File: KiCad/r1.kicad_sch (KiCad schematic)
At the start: 73 parts, among them J1 KEYBOARD, J2 VIDEO OUT, J3 ATX-20, J4 DE9_Socket, J5 R1 EXPANSION, Q1 2N4401, SW1 RESET, SW2 CLEAR, U1 6502, U10 74LS245, U11 MAX232, U2 6821, U3 27C64, U4 HM62256BLP, U5 74LS138, U6 74LS00, U7 74LS04, U8 P8X32A-D40, U9 24LC256, X1 1 MHz, X2 5MHz

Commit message: Unzipped and rearranged directories
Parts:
- added C21: 100, Capacitor_THT:CP_Radial_D10.0mm_P5.00mm, symbol Device:C_Polarized
- added C22: 100, Capacitor_THT:CP_Radial_D5.0mm_P2.50mm, symbol Device:C_Polarized
- added S1: ON/OFF, Button_Switch_THT:SW_PUSH_6mm, symbol Switch:SW_DPST
- D1: value LED -> POWER; footprint (none) -> LED_THT:LED_D5.0mm
- JP1, JP2: footprint (none) -> TestPoint:TestPoint_Bridge_Pitch2.54mm_Drill1.0mm
- S3: renamed from SW2; footprint (none) -> Button_Switch_THT:SW_PUSH_6mm
- renumbered SW1 to S2
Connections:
- net -12V: now also J3.12 (-12V), J5.1 (Pin_1), C22.2
- net A0: now also J5.4 (Pin_4), U3.10 (A0), U4.10 (A0)
- net A1: now also J5.24 (Pin_24), U3.9 (A1), U4.9 (A1)
- net A10: now also J5.9 (Pin_9), U3.21 (A10), U4.21 (A10)
- net A11: now also J5.29 (Pin_29), U3.23 (A11), U4.23 (A11)
- net A12: now also J5.10 (Pin_10), U3.2 (A12), U4.2 (A12), U5.1 (A0)
- net A13: now also J5.30 (Pin_30), U4.26 (A13), U5.2 (A1)
- net A14: now also J5.11 (Pin_11), U4.1 (A14), U5.3 (A2)
- net A15: now also J5.31 (Pin_31), U4.20 (~{CS}), U4.22 (~{OE}), U5.6 (E3)
- net A2: now also J5.5 (Pin_5), U3.8 (A2), U4.8 (A2)
- net A3: now also J5.25 (Pin_25), U3.7 (A3), U4.7 (A3)
- net A4: now also J5.6 (Pin_6), U3.6 (A4), U4.6 (A4)
- net A5: now also J5.26 (Pin_26), U3.5 (A5), U4.5 (A5)
- net A6: now also J5.7 (Pin_7), U3.4 (A6), U4.4 (A6)
- net A7: now also J5.27 (Pin_27), U3.3 (A7), U4.3 (A7)
- net A8: now also J5.8 (Pin_8), U3.25 (A8), U4.25 (A8)
- net A9: now also J5.28 (Pin_28), U3.24 (A9), U4.24 (A9)
- net D0: now also J5.33 (Pin_33), U3.11 (D0), U4.11 (Q0)
- net D1: now also J5.15 (Pin_15), U3.12 (D1), U4.12 (Q1)
- net D2: now also J5.34 (Pin_34), U3.13 (D2), U4.13 (Q2)
- net D3: now also J5.16 (Pin_16), U3.15 (D3), U4.15 (Q3)
- net D4: now also J5.35 (Pin_35), U3.16 (D4), U4.16 (Q4)
- net D5: now also J5.17 (Pin_17), U3.17 (D5), U4.17 (Q5)
- net D6: now also J5.36 (Pin_36), U3.18 (D6), U4.18 (Q6)
- net D7: now also J5.18 (Pin_18), U3.19 (D7), U4.19 (Q7)
- net GND: now also C14.2, C15.2, C19.1, C20.2, C8.1, C9.1, D1.2 (A), J3.13 (GND), J3.15 (GND), J3.16 (GND), J3.17 (GND), J3.3 (GND), J3.5 (GND), J3.7 (GND), J4.5, J5.3 (Pin_3), Q1.3 (E), R24.2, U11.15 (GND), U5.4 (E1), U5.5 (E2), U5.8 (GND), V1.2 (GND), V2.2 (GND), C21.2, C22.1, S1.2; no longer C8.2, C9.2
- net IRQ: now also J5.38 (Pin_38)
- net NMI: now also J5.39 (Pin_39)
- net PHI0: now also J5.23 (Pin_23)
- net PHI1: now also J5.14 (Pin_14)
- net PHI2: now also J5.20 (Pin_20), U6.12
- net RDY: now also J5.37 (Pin_37)
- net RESET: now also J5.40 (Pin_40)
- net RX: now also R18.1
- net R/W: now also J5.12 (Pin_12), U6.4, U6.5
- net SYNC: now also J5.19 (Pin_19)
- net TX: now also U11.11 (T1IN)
- net VCC: now also C14.1, C18.2, C20.1, J3.19 (+5V), J3.20 (+5V), J3.4 (+5V), J3.6 (+5V), J5.21 (Pin_21), R20.2, U11.16 (VCC), U3.27 (~{PGM}), U3.28 (VCC), U4.28 (VCC), U5.16 (VCC), V1.3 (VO), V2.1 (IN)
- net VDD: now also C15.1, C8.2, C9.2, R6.1, V2.3 (OUT); no longer C8.1, C9.1, R6.2
- net at J2.1 (In), R17.1: now also R21.1, R23.2; no longer R18.1, R19.1
- net at R18.2: now also U11.12 (R1OUT); no longer U8.18 (P13)
- net at R23.1: now also U8.18 (P13)
- net at R25.1: now also C13.2
- net at R25.2: now also Q1.2 (B), R24.1
- net at U6.6: now also U6.13
- net RST: now reaches JP2.2 (B), S3.2, U8.11 (~{RES})
- net RST: now also Q1.1 (C)
- net at U8.19 (P14): now also R21.2; no longer R19.2
- net at U8.38 (P29), U9.5 (SDA): now also R6.2; no longer R6.1
- net at U4.27 (~{WE}): now also U6.11
- net at U6.10: now also U6.3, U6.9
- net at U6.8: now also U3.20 (~{CE}), U3.22 (~{OE})
- net at C17.1: now also U11.4 (C2+)
- net at C17.2: now also U11.5 (C2-)
- net at C16.1: now also U11.1 (C1+)
- net at C16.2: now also U11.3 (C1-)
- net at R20.1: now also D1.1 (K)
- net at V1.1 (VI): now also C21.1, S1.4
- net at U11.13 (R1IN): now also J4.3
- net at U11.14 (T1OUT): now also J4.2
- net at U11.2 (VS+): now also C18.1
- net at U11.6 (VS-): now also C19.2
- net $D000: now reaches U5.10 (O5)
- net $C000: now reaches U5.11 (O4)
- net $C000: now also J5.22 (Pin_22)
- net $B000: now reaches U5.12 (O3)
- net $B000: now also J5.32 (Pin_32)
- net $A000: now reaches U5.13 (O2)
- net $A000: now also J5.13 (Pin_13)
- net at U5.7 (O7): now also U6.2
- net at U5.9 (O6): now also U6.1
- net at J4.1: now also J4.6
- net at J4.4: now also C13.1
- net 12V: now reaches J3.10 (+12V)
- net 12V: now also J5.2 (Pin_2)
- net at J3.14 (PS_ON#): now also S1.1
- no-connect marks 10 -> 26
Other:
- moved on the sheet: C13, C14, C15, C16, C17, C18, C19, C20, C8, C9, D1, J1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

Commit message: R20260909
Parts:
- added J6: Mini-DIN-6, symbol Connector:Mini-DIN-6
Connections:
- net GND: now also J6.3
- net KCL: now also R19.1
- net VCC: now also R22.1, J6.4; no longer R20.2
- net VDD: now also R7.1, R8.1
- net at R8.2: now also R20.1, J6.1
- net at R25.1: now also Q1.2 (B), R24.1; no longer C13.2
- net at R19.2: now also R7.2, J6.5
- net at R22.2: now also D1.1 (K)
- new net: C13.2, R25.2
- new net DATA: R20.2
- no-connect marks 26 -> 28
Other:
- moved on the sheet: R19, R20, R22, R25, R7, R8

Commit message: R20260910
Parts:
- added J7: 7-9V DC, Connector_BarrelJack:BarrelJack_GCT_DCJ200-10-A_Horizontal, symbol Connector:Jack-DC
- C22: footprint Capacitor_THT:CP_Radial_D5.0mm_P2.50mm -> Capacitor_THT:CP_Radial_D5.0mm_P2.00mm
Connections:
- net $A000: now also J5.25 (Pin_25); no longer J5.13 (Pin_13)
- net $B000: now also J5.24 (Pin_24); no longer J5.32 (Pin_32)
- net $C000: now also J5.4 (Pin_4); no longer J5.22 (Pin_22)
- net A0: now also J5.7 (Pin_7); no longer J5.4 (Pin_4)
- net A1: now also J5.8 (Pin_8); no longer J5.24 (Pin_24)
- net A10: now also J5.17 (Pin_17); no longer J5.9 (Pin_9)
- net A11: now also J5.18 (Pin_18); no longer J5.29 (Pin_29)
- net A12: now also J5.19 (Pin_19); no longer J5.10 (Pin_10)
- net A13: now also J5.20 (Pin_20); no longer J5.30 (Pin_30)
- net A14: now also J5.21 (Pin_21); no longer J5.11 (Pin_11)
- net A15: now also J5.22 (Pin_22); no longer J5.31 (Pin_31)
- net A2: now also J5.9 (Pin_9); no longer J5.5 (Pin_5)
- net A3: now also J5.10 (Pin_10); no longer J5.25 (Pin_25)
- net A4: now also J5.11 (Pin_11); no longer J5.6 (Pin_6)
- net A5: now also J5.12 (Pin_12); no longer J5.26 (Pin_26)
- net A6: now also J5.13 (Pin_13); no longer J5.7 (Pin_7)
- net A7: now also J5.14 (Pin_14); no longer J5.27 (Pin_27)
- net A8: now also J5.15 (Pin_15); no longer J5.8 (Pin_8)
- net A9: now also J5.16 (Pin_16); no longer J5.28 (Pin_28)
- net D0: now also J5.26 (Pin_26); no longer J5.33 (Pin_33)
- net D1: now also J5.29 (Pin_29); no longer J5.15 (Pin_15)
- net D2: now also J5.28 (Pin_28); no longer J5.34 (Pin_34)
- net D3: now also J5.31 (Pin_31); no longer J5.16 (Pin_16)
- net D4: now also J5.30 (Pin_30); no longer J5.35 (Pin_35)
- net D5: now also J5.33 (Pin_33); no longer J5.17 (Pin_17)
- net D6: now also J5.32 (Pin_32); no longer J5.36 (Pin_36)
- net D7: now also J5.35 (Pin_35); no longer J5.18 (Pin_18)
- net DATA: now also R20.1; no longer R20.2
- net GND: now also J5.5 (Pin_5), R26.1, R5.2, S2.1, U6.7 (GND), U7.7 (GND), X1.7 (GND); no longer J5.3 (Pin_3), R26.2, S2.2
- net IRQ: now also J5.36 (Pin_36); no longer J5.38 (Pin_38)
- net K7: now also R5.1
- net NMI: now also J5.38 (Pin_38); no longer J5.39 (Pin_39)
- net PHI0: now also J5.6 (Pin_6); no longer J5.23 (Pin_23)
- net PHI1: now also J5.27 (Pin_27); no longer J5.14 (Pin_14)
- net PHI2: now also J5.39 (Pin_39); no longer J5.20 (Pin_20)
- net RDY: now also J5.34 (Pin_34); no longer J5.37 (Pin_37)
- net RESET: now also S2.2; no longer S2.1
- net RX: now also R18.2; no longer R18.1
- net R/W: now also J5.23 (Pin_23); no longer J5.12 (Pin_12)
- net STROBE: now also R26.2; no longer R26.1
- net SYNC: now also J5.37 (Pin_37); no longer J5.19 (Pin_19)
- net VCC: now also J5.2 (Pin_2), U6.14 (VCC), U7.14 (VCC), X1.14 (Vcc); no longer J5.21 (Pin_21)
- net at J6.1, R8.2: now also R20.2; no longer R20.1
- net at U11.12 (R1OUT): now also R18.1; no longer R18.2
- net at R23.1: now also J2.1 (In), R17.1, R21.1; no longer U8.18 (P13)
- net 12V renamed +12V
- net +12V: now also J5.3 (Pin_3); no longer J5.2 (Pin_2)
- new net: R23.2, U8.18 (P13)
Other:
- moved on the sheet: C21, R18, R20, R23, R26, R5, S2, U6E, U7G

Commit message: R20260918
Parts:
- removed R27: 1K, Resistor_THT:R_Axial_DIN0207_L6.3mm_D2.5mm_P10.16mm_Horizontal, symbol Device:R
- J2: footprint (none) -> r1te:Keystone 901
- JP1, JP2: value SolderJumper_2_Open -> Jumper_2_Open; symbol Jumper:SolderJumper_2_Open -> Jumper:Jumper_2_Open; now in the parts list
- S1: footprint Button_Switch_THT:SW_PUSH_6mm -> r1te:ToggleSW_DPDT_VerticalPC
- U6: footprint Package_DIP:DIP-16_W7.62mm_Socket_LongPads -> Package_DIP:DIP-14_W7.62mm_Socket_LongPads
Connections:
- net $D00 is gone; now on net $D000: U2.23 (~{CS2})
- net GND: now also J7.2
- net PB0: now also U2.10 (PB0)
- net PB1: now also R10.1; no longer R10.2
- net PHI0: now also X1.8 (OUT)
- net at U8.2 (P1): now also R10.2; no longer R10.1
- net at U8.30 (XI): now also X2.2; no longer X2.1
- net at U8.31 (XO): now also X2.1; no longer X2.2
- net at S1.3: now also J7.1
- no-connect marks 28 -> 29
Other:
- moved on the sheet: C14, C15, C21, J7, R10, V1, V2, X1

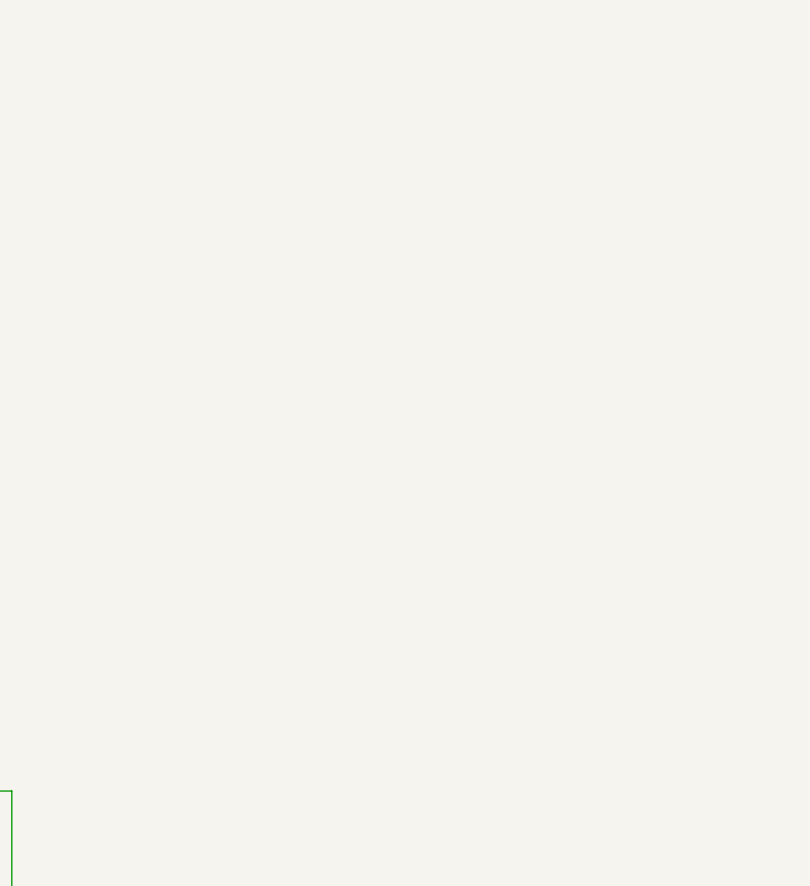
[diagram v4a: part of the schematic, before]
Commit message: Create edge finger footprints and trace cleanup
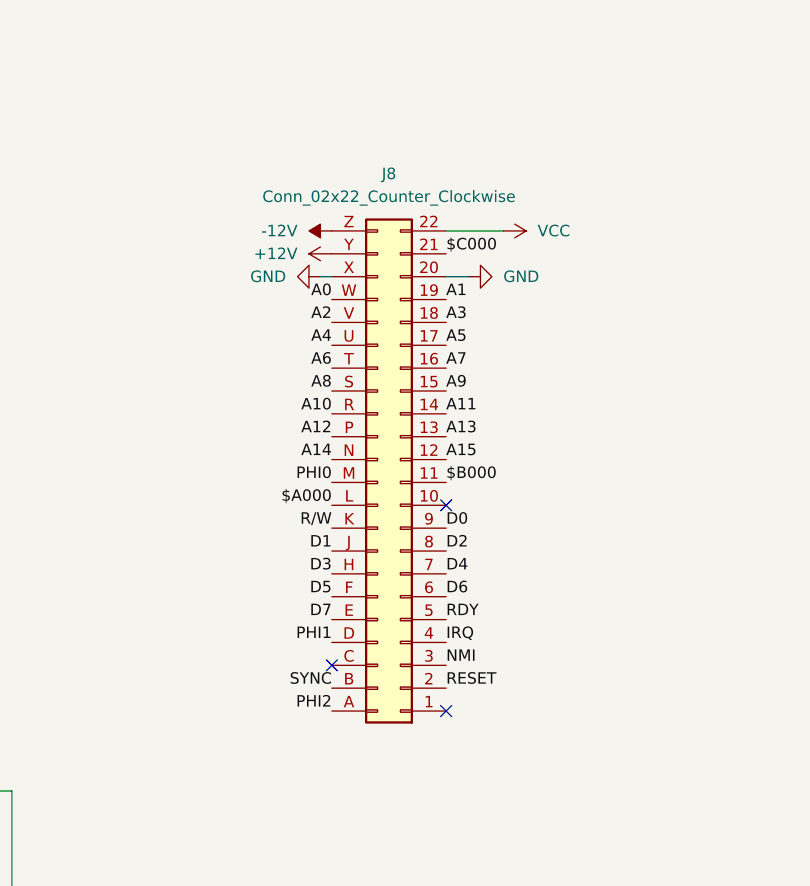
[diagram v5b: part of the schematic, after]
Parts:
- added J8: Conn_02x22_Counter_Clockwise, r1te:CardEdgeConnector_44p_P156mils, symbol a1symbols:Conn_02x22_edgecon
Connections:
- net $A000: now also J8.L (Pin_3L)
- net $B000: now also J8.11 (Pin_11)
- net $C000: now also J8.21 (Pin_21)
- net +12V: now also J8.Y (Pin_Y)
- net -12V: now also J8.Z (Pin_Z)
- net A0: now also J8.W (Pin_W)
- net A1: now also J8.19 (Pin_19)
- net A10: now also J8.R (Pin_R)
- net A11: now also J8.14 (Pin_14)
- net A12: now also J8.P (Pin_P)
- net A13: now also J8.13 (Pin_13)
- net A14: now also J8.N (Pin_N)
- net A15: now also J8.12 (Pin_12)
- net A2: now also J8.V (Pin_V)
- net A3: now also J8.18 (Pin_18)
- net A4: now also J8.U (Pin_U)
- net A5: now also J8.17 (Pin_17)
- net A6: now also J8.T (Pin_T)
- net A7: now also J8.16 (Pin_16)
- net A8: now also J8.S (Pin_S)
- net A9: now also J8.15 (Pin_15)
- net D0: now also J8.9 (Pin_9)
- net D1: now also J8.J (Pin_J)
- net D2: now also J8.8 (Pin_8)
- net D3: now also J8.H (Pin_H)
- net D4: now also J8.7 (Pin_7)
- net D5: now also J8.F (Pin_F)
- net D6: now also J8.6 (Pin_6)
- net D7: now also J8.E (Pin_E)
- net GND: now also J8.20 (Pin_20), J8.X (Pin_X)
- net IRQ: now also J8.4 (Pin_4)
- net NMI: now also J8.3 (Pin_3)
- net PHI0: now also J8.M (Pin_M)
- net PHI1: now also J8.D (Pin_D)
- net PHI2: now also J8.A (Pin_A)
- net RDY: now also J8.5 (Pin_5)
- net RESET: now also J8.2 (Pin_2)
- net R/W: now also J8.K (Pin_K)
- net SYNC: now also J8.B (PinB)
- net VCC: now also J8.22 (Pin_22)
- no-connect marks 29 -> 32
